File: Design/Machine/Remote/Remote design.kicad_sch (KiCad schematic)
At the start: 28 parts, among them SW1 PAuto, SW10 SwitchScores, SW11 PManual, SW12 YCardR, SW13 RCardR, SW14 IncPeriod, SW15 DecRight, SW16 IncRight, SW17 ThreeMin, SW18 DecTime, SW19 CycleTime, SW2 Block, SW20 PauseRes, SW21 Upload, SW22 ON-OFF, SW3 YCardL, SW4 RCardL, SW5 DecLeft, SW6 IncLeft, SW7 OneMin, SW8 IncTime, SW9 ResetMachine

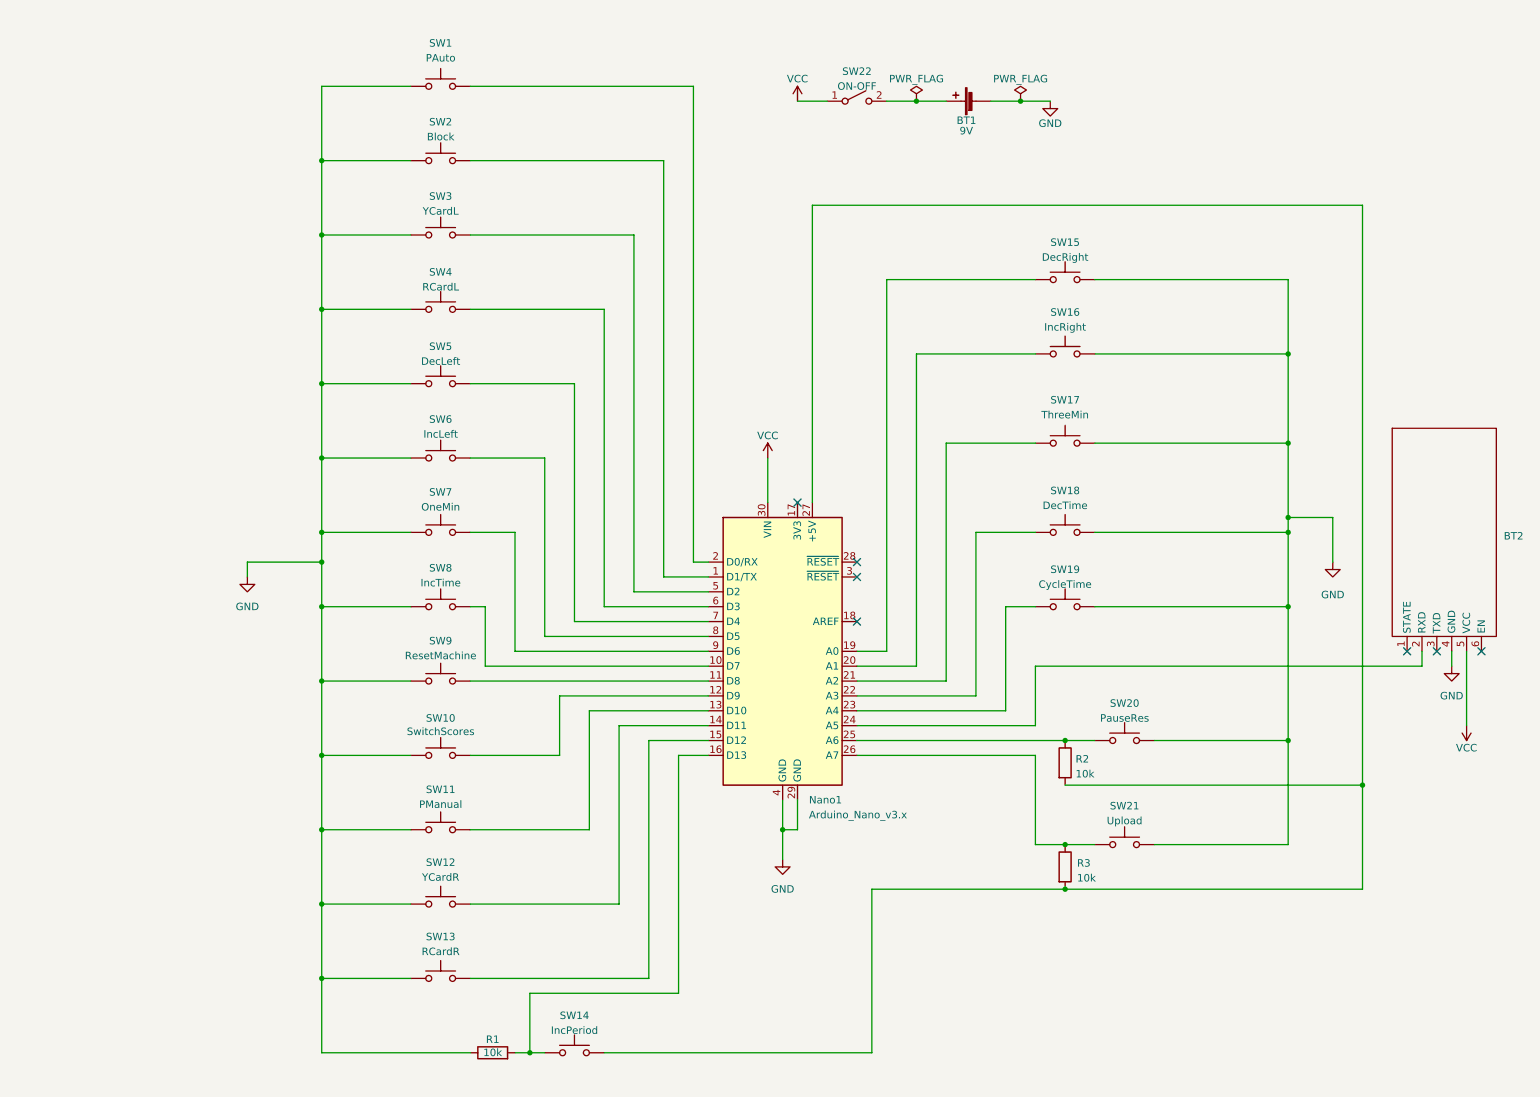
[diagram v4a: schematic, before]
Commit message: feat: new buttons, Arduino Mega, nrf24L01
rewire new buttons and replace Arduino Nano with Arduino MEGA and replace 315MHz with nRF24L01
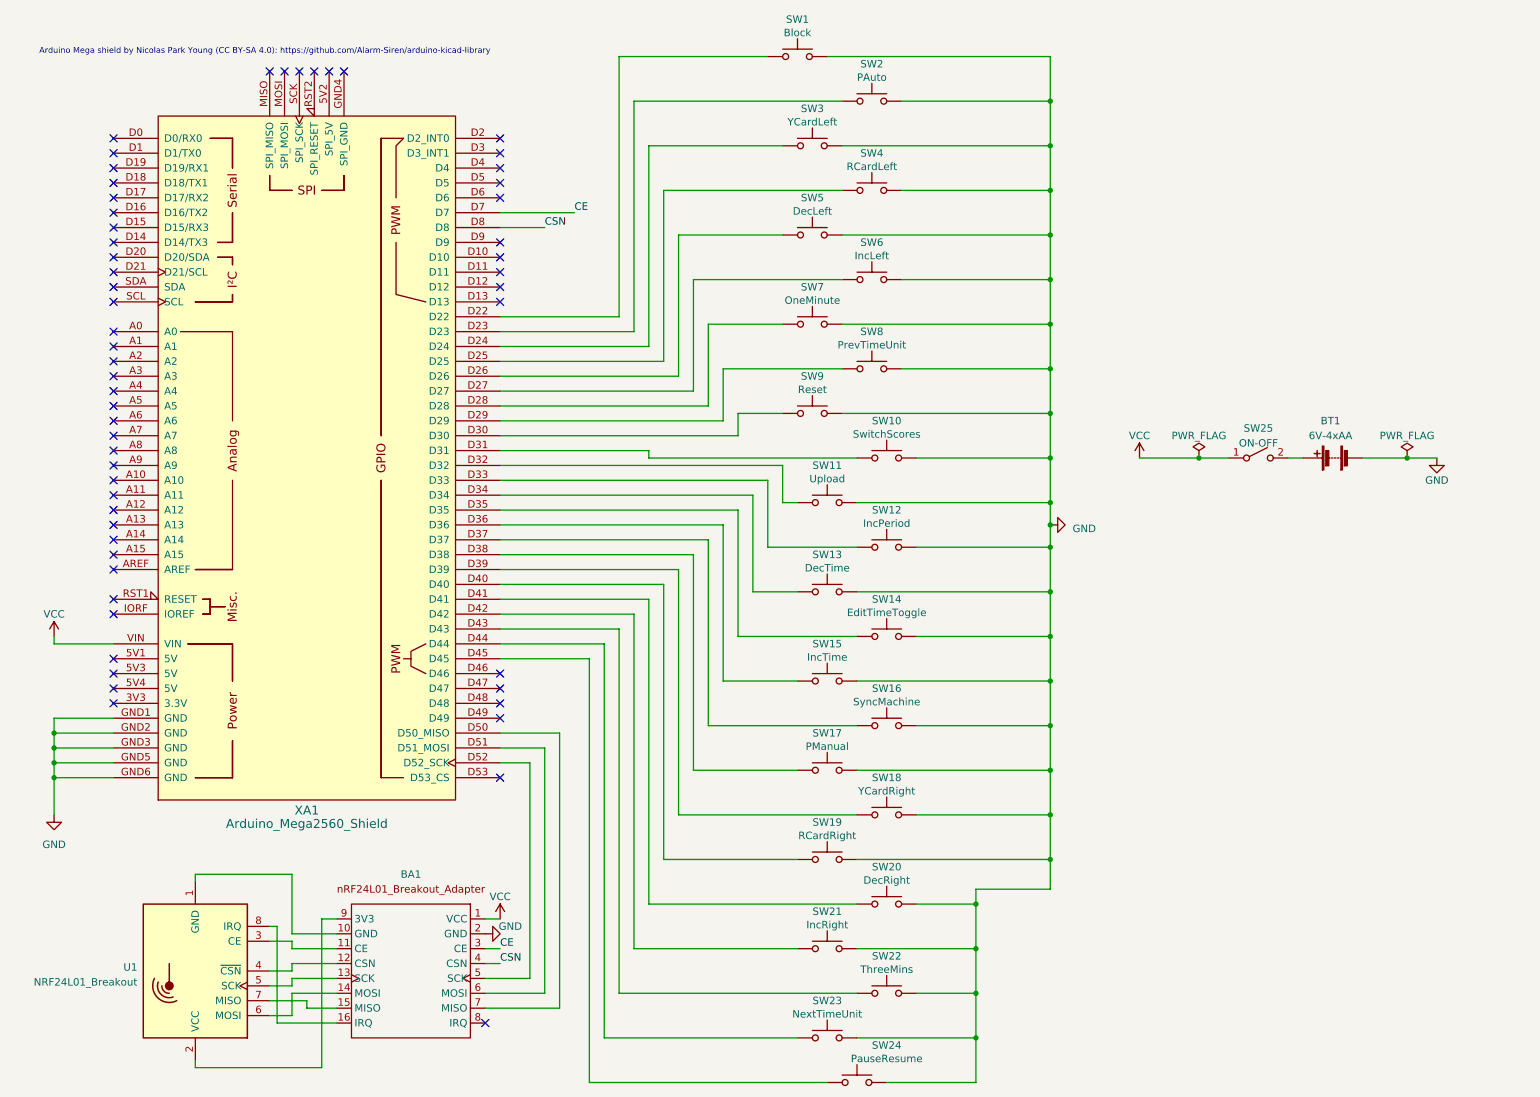
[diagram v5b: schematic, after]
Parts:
- removed BT1: 9V, Connector_PinHeader_2.54mm:PinHeader_1x02_P2.54mm_Vertical, symbol Device:Battery_Cell
- removed BT2: ~, symbol Arduino modules:ZS-040_HC-05
- removed Nano1: Arduino_Nano_v3.x, Module:Arduino_Nano, symbol MCU_Module:Arduino_Nano_v3.x
- removed R1, R2, R3: 10k, Resistor_THT:R_Axial_DIN0207_L6.3mm_D2.5mm_P10.16mm_Horizontal, symbol Device:R
- removed SW1: PAuto, Button_Switch_THT:SW_PUSH_6mm, symbol Switch:SW_Push
- added BA1: ~, Connector_PinSocket_2.54mm:PinSocket_1x08_P2.54mm_Vertical, symbol Arduino modules:nRF24L01_Breakout_Adapter_with_Voltage_Regulator
- added BT1: 6V-4xAA, Connector_PinHeader_2.54mm:PinHeader_1x02_P2.54mm_Vertical, symbol Device:Battery
- added SW15: IncTime, Button_Switch_THT:SW_PUSH_6mm, symbol Switch:SW_Push
- added SW22: ThreeMins, Button_Switch_THT:SW_PUSH_6mm, symbol Switch:SW_Push
- added SW23: NextTimeUnit, Button_Switch_THT:SW_PUSH_6mm, symbol Switch:SW_Push
- added SW24: PauseResume, Button_Switch_THT:SW_PUSH_6mm, symbol Switch:SW_Push
- added U1: NRF24L01_Breakout, RF_Module:nRF24L01_Breakout, symbol RF:NRF24L01_Breakout
- added XA1: Arduino_Mega2560_Shield, PCM_arduino-library:Arduino_Mega2560_Shield, symbol PCM_arduino-library:Arduino_Mega2560_Shield
- SW1: renamed from SW15; value DecRight -> Block
- SW11: value PManual -> Upload
- SW12: value YCardR -> IncPeriod
- SW13: value RCardR -> DecTime
- SW14: value IncPeriod -> EditTimeToggle
- SW16: value IncRight -> SyncMachine
- SW17: value ThreeMin -> PManual
- SW18: value DecTime -> YCardRight
- SW19: value CycleTime -> RCardRight
- SW2: value Block -> PAuto
- SW20: value PauseRes -> DecRight
- SW21: value Upload -> IncRight
- SW3: value YCardL -> YCardLeft
- SW4: value RCardL -> RCardLeft
- SW7: value OneMin -> OneMinute
- SW8: value IncTime -> PrevTimeUnit
- SW9: value ResetMachine -> Reset
- renumbered SW22 to SW25
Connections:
- net GND: now also SW10.2, SW11.2, SW12.2, SW13.2, SW14.2, SW2.2, SW3.2, SW4.2, SW5.2, SW6.2, SW7.2, SW8.2, SW9.2, BA1.2 (GND), BT1.2 (-), SW15.2, SW22.2, SW23.2, SW24.2, XA1.GND1 (GND), XA1.GND2 (GND), XA1.GND3 (GND), XA1.GND5 (GND), XA1.GND6 (GND); no longer SW10.1, SW11.1, SW12.1, SW13.1, SW2.1, SW3.1, SW4.1, SW5.1, SW6.1, SW7.1, SW8.1, SW9.1
- net VCC: now also BA1.1 (VCC), XA1.VIN
- net at SW20.1: now also XA1.D41
- net at SW1.1: now also XA1.D22
- net at SW14.1: now also XA1.D35
- net at SW19.1: now also XA1.D40
- net at SW16.1: now also XA1.D37
- net at SW18.1: now also XA1.D39
- net at SW21.1: now also XA1.D42
- net at SW25.2 (B): now also BT1.1 (+)
- net at SW17.1: now also XA1.D38
- new net: SW2.1, XA1.D23
- new net: SW3.1, XA1.D24
- new net: SW4.1, XA1.D25
- new net: SW5.1, XA1.D26
- new net: SW6.1, XA1.D27
- new net: SW7.1, XA1.D28
- new net: SW8.1, XA1.D29
- new net: SW9.1, XA1.D30
- new net: SW10.1, XA1.D31
- new net: SW11.1, XA1.D32
- new net: SW12.1, XA1.D33
- new net: SW13.1, XA1.D34
- new net: SW15.1, XA1.D36
- new net: SW22.1, XA1.D43
- new net: SW23.1, XA1.D44
- new net: SW24.1, XA1.D45
- new net: BA1.7 (MISO), XA1.D50 (D50_MISO)
- new net: BA1.6 (MOSI), XA1.D51 (D51_MOSI)
- new net: BA1.5 (SCK), XA1.D52 (D52_SCK)
- new net: BA1.10 (GND), U1.1 (GND)
- new net: BA1.11 (CE), U1.3 (CE)
- new net: BA1.12 (CSN), U1.4 (~{CSN})
- new net: BA1.13 (SCK), U1.5 (SCK)
- new net: BA1.14 (MOSI), U1.6 (MOSI)
- new net: BA1.15 (MISO), U1.7 (MISO)
- new net: BA1.16 (IRQ), U1.8 (IRQ)
- new net: BA1.9 (3V3), U1.2 (VCC)
- new net CE: BA1.3 (CE), XA1.D7
- new net CSN: BA1.4 (CSN), XA1.D8
- no-connect marks 7 -> 57
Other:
- note added: "Arduino Mega shield by Nicolas Park Young (CC BY-SA 4.0): https://github.com/Alarm-Siren/arduino-kicad-library"
- moved on the sheet: SW1, SW25

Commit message: feat: logic unit schematics
make schematics for logic unit, power redundancy unit still missing
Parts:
- U1: footprint RF_Module:nRF24L01_Breakout -> (none)
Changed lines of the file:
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@@
       (effects (font (size 1.27 1.27)) (justify left))
     )
-    (property "Footprint" "RF_Module:nRF24L01_Breakout" (at 38.1 191.77 0)
+    (property "Footprint" "" (at 38.1 191.77 0)
       (effects (font (size 1.27 1.27) italic) (justify left) hide)
     )

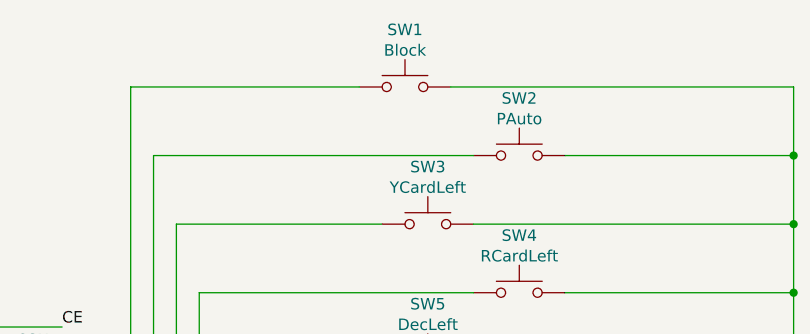
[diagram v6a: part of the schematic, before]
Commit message: feat: complete remote logic
implement complete logic for remote commands, also make block button now reset the cards (useful for teams competitions)
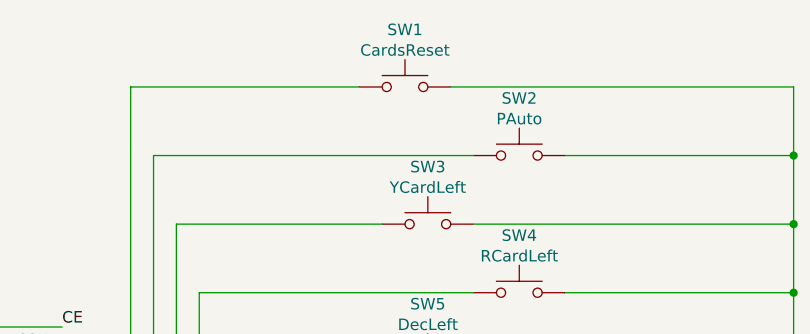
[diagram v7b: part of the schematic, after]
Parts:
- SW1: value Block -> CardsReset
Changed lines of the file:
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@@
       (effects (font (size 1.27 1.27)))
     )
-    (property "Value" "Block" (at 144.78 16.256 0)
+    (property "Value" "CardsReset" (at 144.78 16.256 0)
       (effects (font (size 1.27 1.27)))
     )

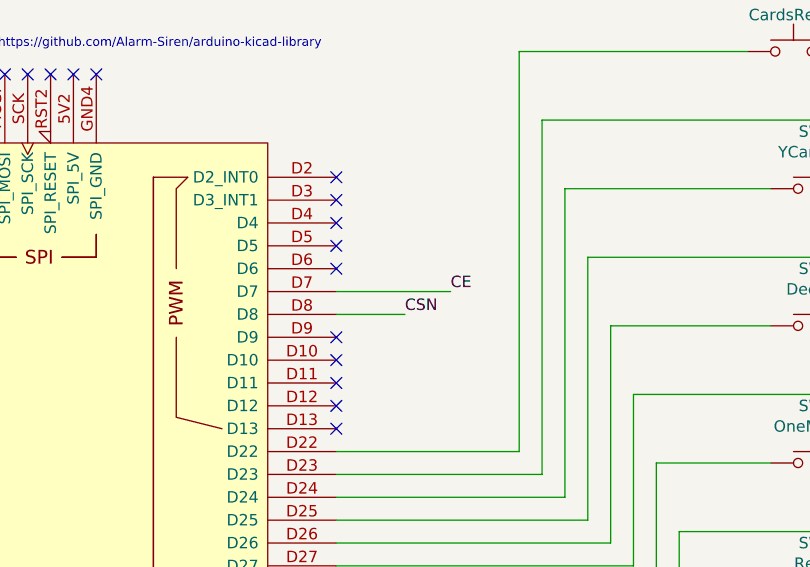
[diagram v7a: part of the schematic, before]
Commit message: fix: remote controller SPI pins
change CE and CSN pins so that they are a better fit in a  perfboard
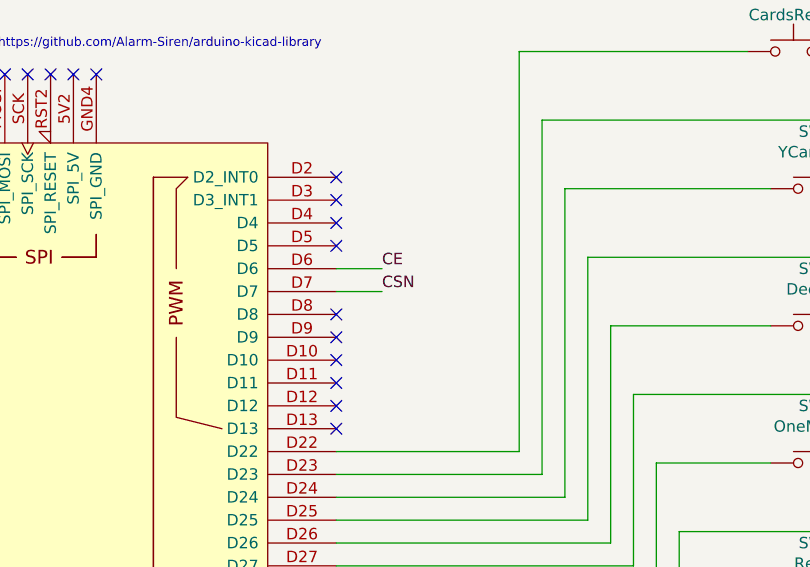
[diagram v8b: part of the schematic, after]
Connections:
- net CE: now also XA1.D6; no longer XA1.D7
- net CSN: now also XA1.D7; no longer XA1.D8
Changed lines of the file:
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@@
   (no_connect (at 27.94 34.29))
   (no_connect (at 91.44 185.42))
-  (no_connect (at 93.98 44.45))
   (no_connect (at 27.94 90.17))
   (no_connect (at 27.94 72.39))
@@
   (no_connect (at 93.98 39.37))
   (no_connect (at 27.94 54.61))
+  (no_connect (at 93.98 49.53))
   (no_connect (at 27.94 69.85))
   (no_connect (at 27.94 49.53))
@@
     (stroke (width 0) (type default))
   )
+  (wire (pts (xy 93.98 46.99) (xy 99.06 46.99))
+    (stroke (width 0) (type default))
+  )
   (wire (pts (xy 119.38 88.9) (xy 154.94 88.9))
     (stroke (width 0) (type default))
@@
     (stroke (width 0) (type default))
   )
+  (wire (pts (xy 93.98 44.45) (xy 99.06 44.45))
+    (stroke (width 0) (type default))
+  )
   (wire (pts (xy 17.78 140.97) (xy 17.78 143.51))
     (stroke (width 0) (type default))
@@
     (stroke (width 0) (type default))
   )
-  (wire (pts (xy 93.98 46.99) (xy 106.68 46.99))
-    (stroke (width 0) (type default))
-  )
   (wire (pts (xy 114.3 64.77) (xy 114.3 20.32))
     (stroke (width 0) (type default))
@@
   )
   (wire (pts (xy 93.98 120.65) (xy 111.76 120.65))
-    (stroke (width 0) (type default))
-  )
-  (wire (pts (xy 101.6 49.53) (xy 93.98 49.53))
     (stroke (width 0) (type default))
   )
@@
     (effects (font (size 1.27 1.27)) (justify left bottom))
   )
-  (label "CSN" (at 101.6 49.53 0) (fields_autoplaced)
+  (label "CSN" (at 99.06 46.99 0) (fields_autoplaced)
     (effects (font (size 1.27 1.27)) (justify left bottom))
   )
@@
     (effects (font (size 1.27 1.27)) (justify left bottom))
   )
-  (label "CE" (at 106.68 46.99 0) (fields_autoplaced)
+  (label "CE" (at 99.06 44.45 0) (fields_autoplaced)
     (effects (font (size 1.27 1.27)) (justify left bottom))
   )
